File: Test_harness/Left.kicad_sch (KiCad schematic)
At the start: 126 parts

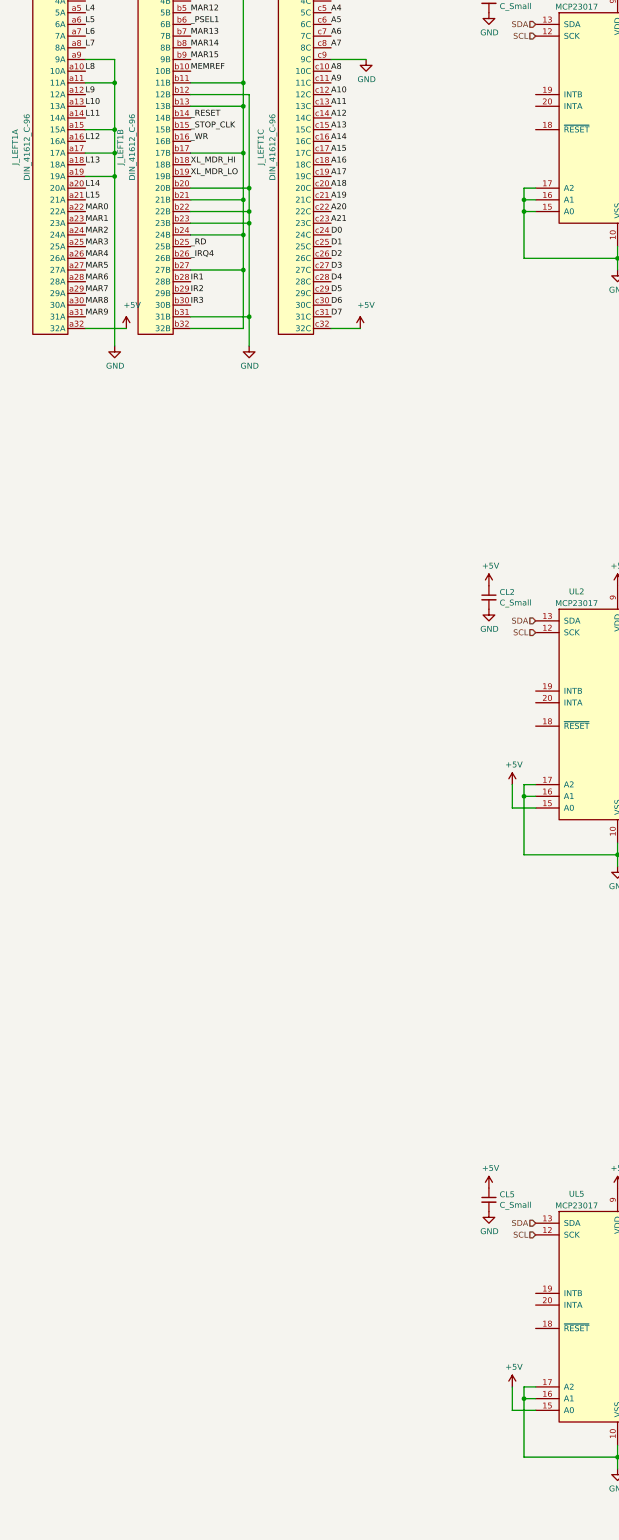
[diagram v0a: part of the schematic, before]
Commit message: route the left connector of test_harness board
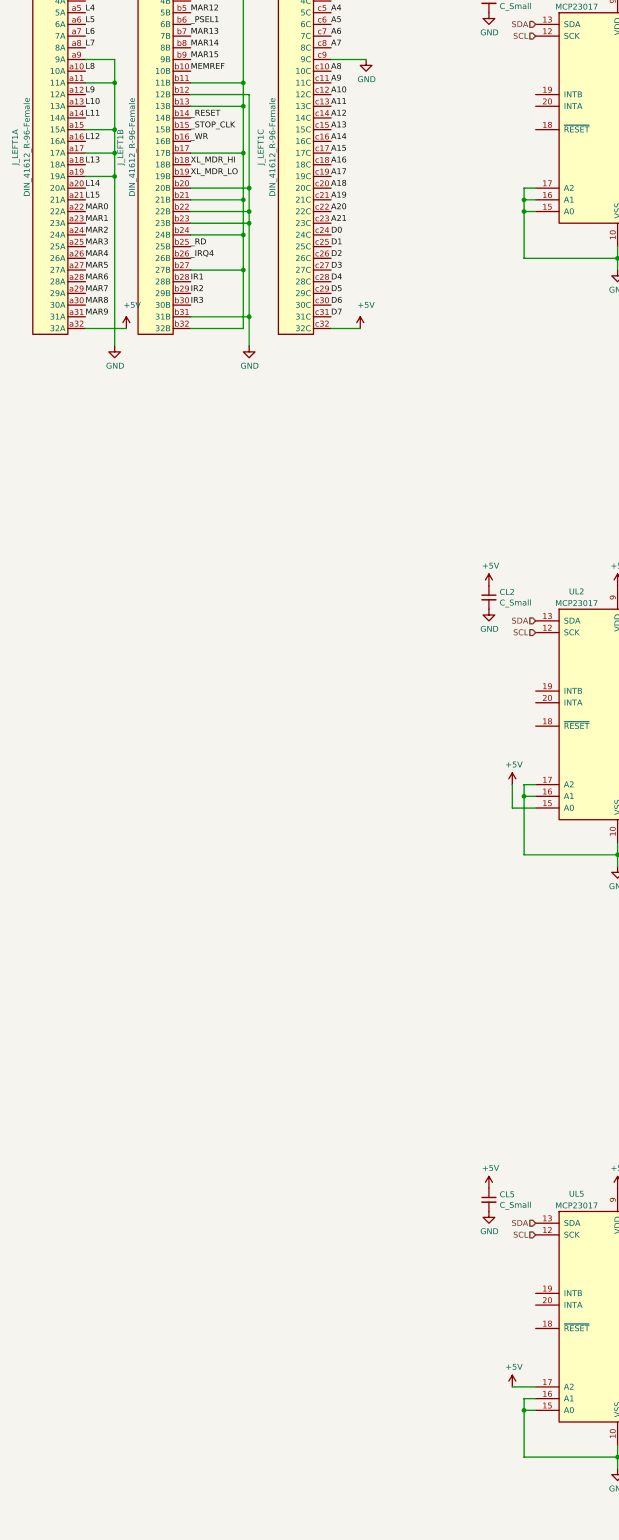
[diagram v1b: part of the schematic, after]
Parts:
- CL1, CL1_1, CL1_2, CL2, CL2_1, CL2_2, CL3, CL3_1, CL3_2, CL4, CL4_1, CL4_2, CL5, CL5_1, CL5_2: footprint Capacitor_SMD:C_1206_3216Metric -> Capacitor_SMD:C_0805_2012Metric
- J_LEFT1: value DIN_41612_C-96 -> DIN_41612_R-96-Female
- UL2: footprint Package_SO:SOIC-28W_7.5x17.9mm_P1.27mm -> Package_SO:TSSOP-28_4.4x9.7mm_P0.65mm
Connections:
- net +5V: now also UL5.17 (A2); no longer UL5.15 (A0)
- net GND: now also UL5.15 (A0); no longer UL5.17 (A2)
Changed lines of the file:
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@@
   (junction (at 128.27 69.85) (diameter 1.016) (color 0 0 0 0))
   (junction (at 128.27 196.85) (diameter 1.016) (color 0 0 0 0))
-  (junction (at 128.27 327.66) (diameter 1.016) (color 0 0 0 0))
+  (junction (at 128.27 330.2) (diameter 1.016) (color 0 0 0 0))
   (junction (at 148.59 80.01) (diameter 1.016) (color 0 0 0 0))
   (junction (at 148.59 209.55) (diameter 1.016) (color 0 0 0 0))
@@
     (stroke (width 0) (type solid) (color 0 0 0 0))
   )
-  (wire (pts (xy 125.73 325.12) (xy 125.73 330.2))
+  (wire (pts (xy 125.73 325.12) (xy 130.81 325.12))
     (stroke (width 0) (type solid) (color 0 0 0 0))
   )
@@
     (stroke (width 0) (type solid) (color 0 0 0 0))
   )
-  (wire (pts (xy 128.27 325.12) (xy 128.27 327.66))
+  (wire (pts (xy 128.27 327.66) (xy 128.27 330.2))
     (stroke (width 0) (type solid) (color 0 0 0 0))
   )
-  (wire (pts (xy 128.27 327.66) (xy 128.27 340.36))
+  (wire (pts (xy 128.27 327.66) (xy 130.81 327.66))
     (stroke (width 0) (type solid) (color 0 0 0 0))
   )
-  (wire (pts (xy 128.27 327.66) (xy 130.81 327.66))
+  (wire (pts (xy 128.27 330.2) (xy 128.27 340.36))
+    (stroke (width 0) (type solid) (color 0 0 0 0))
+  )
+  (wire (pts (xy 128.27 330.2) (xy 130.81 330.2))
     (stroke (width 0) (type solid) (color 0 0 0 0))
   )
@@
     (stroke (width 0) (type solid) (color 0 0 0 0))
   )
-  (wire (pts (xy 130.81 325.12) (xy 128.27 325.12))
-    (stroke (width 0) (type solid) (color 0 0 0 0))
-  )
-  (wire (pts (xy 130.81 330.2) (xy 125.73 330.2))
-    (stroke (width 0) (type solid) (color 0 0 0 0))
-  )
   (wire (pts (xy 148.59 77.47) (xy 148.59 80.01))
     (stroke (width 0) (type solid) (color 0 0 0 0))
@@
       (effects (font (size 1.27 1.27)) (justify left))
     )
-    (property "Footprint" "Capacitor_SMD:C_1206_3216Metric" (id 2) (at 120.65 24.13 0)
+    (property "Footprint" "Capacitor_SMD:C_0805_2012Metric" (id 2) (at 120.65 24.13 0)
       (effects (font (size 1.27 1.27)) hide)
     )
@@
       (effects (font (size 1.27 1.27)) (justify left))
     )
-    (property "Footprint" "Capacitor_SMD:C_1206_3216Metric" (id 2) (at 120.65 153.67 0)
+    (property "Footprint" "Capacitor_SMD:C_0805_2012Metric" (id 2) (at 120.65 153.67 0)
       (effects (font (size 1.27 1.27)) hide)
     )
@@
       (effects (font (size 1.27 1.27)) (justify left))
     )
-    (property "Footprint" "Capacitor_SMD:C_1206_3216Metric" (id 2) (at 120.65 284.48 0)
+    (property "Footprint" "Capacitor_SMD:C_0805_2012Metric" (id 2) (at 120.65 284.48 0)
       (effects (font (size 1.27 1.27)) hide)
     )
@@
       (effects (font (size 1.27 1.27)) (justify left))
     )
-    (property "Footprint" "Capacitor_SMD:C_1206_3216Metric" (id 2) (at 176.53 21.59 0)
+    (property "Footprint" "Capacitor_SMD:C_0805_2012Metric" (id 2) (at 176.53 21.59 0)
       (effects (font (size 1.27 1.27)) hide)
     )
@@
       (effects (font (size 1.27 1.27)) (justify left))
     )
-    (property "Footprint" "Capacitor_SMD:C_1206_3216Metric" (id 2) (at 176.53 85.09 0)
+    (property "Footprint" "Capacitor_SMD:C_0805_2012Metric" (id 2) (at 176.53 85.09 0)
       (effects (font (size 1.27 1.27)) hide)
     )
@@
       (effects (font (size 1.27 1.27)) (justify left))
     )
-    (property "Footprint" "Capacitor_SMD:C_1206_3216Metric" (id 2) (at 176.53 151.13 0)
+    (property "Footprint" "Capacitor_SMD:C_0805_2012Metric" (id 2) (at 176.53 151.13 0)
       (effects (font (size 1.27 1.27)) hide)
     )
@@
       (effects (font (size 1.27 1.27)) (justify left))
     )
-    (property "Footprint" "Capacitor_SMD:C_1206_3216Metric" (id 2) (at 176.53 214.63 0)
+    (property "Footprint" "Capacitor_SMD:C_0805_2012Metric" (id 2) (at 176.53 214.63 0)
       (effects (font (size 1.27 1.27)) hide)
     )
@@
       (effects (font (size 1.27 1.27)) (justify left))
     )
-    (property "Footprint" "Capacitor_SMD:C_1206_3216Metric" (id 2) (at 185.42 280.67 0)
+    (property "Footprint" "Capacitor_SMD:C_0805_2012Metric" (id 2) (at 185.42 280.67 0)
       (effects (font (size 1.27 1.27)) hide)
     )
@@
       (effects (font (size 1.27 1.27)) (justify left))
     )
-    (property "Footprint" "Capacitor_SMD:C_1206_3216Metric" (id 2) (at 185.42 344.17 0)
+    (property "Footprint" "Capacitor_SMD:C_0805_2012Metric" (id 2) (at 185.42 344.17 0)
       (effects (font (size 1.27 1.27)) hide)
     )
@@
       (effects (font (size 1.27 1.27)) (justify left))
     )
-    (property "Footprint" "Capacitor_SMD:C_1206_3216Metric" (id 2) (at 331.47 26.67 0)
+    (property "Footprint" "Capacitor_SMD:C_0805_2012Metric" (id 2) (at 331.47 26.67 0)
       (effects (font (size 1.27 1.27)) hide)
     )
@@
       (effects (font (size 1.27 1.27)) (justify left))
     )
-    (property "Footprint" "Capacitor_SMD:C_1206_3216Metric" (id 2) (at 331.47 156.21 0)
+    (property "Footprint" "Capacitor_SMD:C_0805_2012Metric" (id 2) (at 331.47 156.21 0)
       (effects (font (size 1.27 1.27)) hide)
     )
@@
       (effects (font (size 1.27 1.27)) (justify left))
     )
-    (property "Footprint" "Capacitor_SMD:C_1206_3216Metric" (id 2) (at 387.35 24.13 0)
+    (property "Footprint" "Capacitor_SMD:C_0805_2012Metric" (id 2) (at 387.35 24.13 0)
       (effects (font (size 1.27 1.27)) hide)
     )
@@
       (effects (font (size 1.27 1.27)) (justify left))
     )
-    (property "Footprint" "Capacitor_SMD:C_1206_3216Metric" (id 2) (at 387.35 87.63 0)
+    (property "Footprint" "Capacitor_SMD:C_0805_2012Metric" (id 2) (at 387.35 87.63 0)
       (effects (font (size 1.27 1.27)) hide)
     )
@@
       (effects (font (size 1.27 1.27)) (justify left))
     )
-    (property "Footprint" "Capacitor_SMD:C_1206_3216Metric" (id 2) (at 387.35 153.67 0)
+    (property "Footprint" "Capacitor_SMD:C_0805_2012Metric" (id 2) (at 387.35 153.67 0)
       (effects (font (size 1.27 1.27)) hide)
     )
@@
       (effects (font (size 1.27 1.27)) (justify left))
     )
-    (property "Footprint" "Capacitor_SMD:C_1206_3216Metric" (id 2) (at 387.35 217.17 0)
+    (property "Footprint" "Capacitor_SMD:C_0805_2012Metric" (id 2) (at 387.35 217.17 0)
       (effects (font (size 1.27 1.27)) hide)
     )
@@
     (in_bom yes) (on_board yes)
     (property "Reference" "J_LEFT1" (id 0) (at 17.78 55.88 90))
-    (property "Value" "DIN_41612_C-96" (id 1) (at 20.32 55.88 90))
+    (property "Value" "DIN_41612_R-96-Female" (id 1) (at 20.32 55.88 90))
     (property "Footprint" "Connector_DIN:DIN41612_C_3x32_Male_Horizontal_THT" (id 2) (at 25.4 54.61 0)
       (effects (font (size 1.27 1.27)) hide)
@@
     (in_bom yes) (on_board yes)
     (property "Reference" "J_LEFT1" (id 0) (at 40.64 55.88 90))
-    (property "Value" "DIN_41612_C-96" (id 1) (at 43.18 55.88 90))
+    (property "Value" "DIN_41612_R-96-Female" (id 1) (at 43.18 55.88 90))
     (property "Footprint" "Connector_DIN:DIN41612_C_3x32_Male_Horizontal_THT" (id 2) (at 48.26 54.61 0)
       (effects (font (size 1.27 1.27)) hide)
@@
     (in_bom yes) (on_board yes)
     (property "Reference" "J_LEFT1" (id 0) (at 71.12 55.88 90))
-    (property "Value" "DIN_41612_C-96" (id 1) (at 73.66 55.88 90))
+    (property "Value" "DIN_41612_R-96-Female" (id 1) (at 73.66 55.88 90))
     (property "Footprint" "Connector_DIN:DIN41612_C_3x32_Male_Horizontal_THT" (id 2) (at 78.74 54.61 0)
       (effects (font (size 1.27 1.27)) hide)
@@
     (property "Reference" "UL2" (id 0) (at 139.7 152.4 0))
     (property "Value" "MCP23017" (id 1) (at 139.7 154.94 0))
-    (property "Footprint" "Package_SO:SOIC-28W_7.5x17.9mm_P1.27mm" (id 2) (at 153.67 204.47 0)
+    (property "Footprint" "Package_SO:TSSOP-28_4.4x9.7mm_P0.65mm" (id 2) (at 153.67 204.47 0)
       (effects (font (size 1.27 1.27)) (justify left) hide)
     )

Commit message: the left connector side of the test harness is in good shape.. even discovered that we can have those HP displays now made by broadcom
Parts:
- added DSP_A0, DSP_A1, DSP_A2, DSP_A3, DSP_A4, DSP_A5, DSP_D0, DSP_D1, DSP_L0, DSP_L1, DSP_L2, DSP_L3: HDSP-0762, Components:HDSP-076x-077x-086x-096x, symbol Magic1_components:HDSP-0762
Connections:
- net +5V: now also DSP_A0.7 (Vcc), DSP_A1.7 (Vcc), DSP_A2.7 (Vcc), DSP_A3.7 (Vcc), DSP_A4.7 (Vcc), DSP_A5.7 (Vcc), DSP_D0.7 (Vcc), DSP_D1.7 (Vcc), DSP_L0.7 (Vcc), DSP_L1.7 (Vcc), DSP_L2.7 (Vcc), DSP_L3.7 (Vcc)
- net D_A0: now also DSP_A0.1 (D1)
- net D_A1: now also DSP_A0.8 (D0)
- net D_A10: now also DSP_A3.3 (D3)
- net D_A11: now also DSP_A3.2 (D2)
- net D_A12: now also DSP_A3.1 (D1)
- net D_A13: now also DSP_A3.8 (D0)
- net D_A14: now also DSP_A4.3 (D3)
- net D_A15: now also DSP_A4.2 (D2)
- net D_A16: now also DSP_A4.1 (D1)
- net D_A17: now also DSP_A4.8 (D0)
- net D_A18: now also DSP_A5.3 (D3)
- net D_A19: now also DSP_A5.2 (D2)
- net D_A2: now also DSP_A1.3 (D3)
- net D_A20: now also DSP_A5.1 (D1)
- net D_A21: now also DSP_A5.8 (D0)
- net D_A3: now also DSP_A1.2 (D2)
- net D_A4: now also DSP_A1.1 (D1)
- net D_A5: now also DSP_A1.8 (D0)
- net D_A6: now also DSP_A2.3 (D3)
- net D_A7: now also DSP_A2.2 (D2)
- net D_A8: now also DSP_A2.1 (D1)
- net D_A9: now also DSP_A2.8 (D0)
- net D_D0: now also DSP_D0.3 (D3)
- net D_D1: now also DSP_D0.2 (D2)
- net D_D2: now also DSP_D0.1 (D1)
- net D_D3: now also DSP_D0.8 (D0)
- net D_D4: now also DSP_D1.3 (D3)
- net D_D5: now also DSP_D1.2 (D2)
- net D_D6: now also DSP_D1.1 (D1)
- net D_D7: now also DSP_D1.8 (D0)
- net D_L0: now also DSP_L0.3 (D3)
- net D_L1: now also DSP_L0.2 (D2)
- net D_L10: now also DSP_L2.1 (D1)
- net D_L11: now also DSP_L2.8 (D0)
- net D_L12: now also DSP_L3.3 (D3)
- net D_L13: now also DSP_L3.2 (D2)
- net D_L14: now also DSP_L3.1 (D1)
- net D_L15: now also DSP_L3.8 (D0)
- net D_L2: now also DSP_L0.1 (D1)
- net D_L3: now also DSP_L0.8 (D0)
- net D_L4: now also DSP_L1.3 (D3)
- net D_L5: now also DSP_L1.2 (D2)
- net D_L6: now also DSP_L1.1 (D1)
- net D_L7: now also DSP_L1.8 (D0)
- net D_L8: now also DSP_L2.3 (D3)
- net D_L9: now also DSP_L2.2 (D2)
- net GND: now also DSP_A0.2 (D2), DSP_A0.3 (D3), DSP_A0.4 (Blk), DSP_A0.6 (GND), DSP_A1.4 (Blk), DSP_A1.6 (GND), DSP_A2.4 (Blk), DSP_A2.6 (GND), DSP_A3.4 (Blk), DSP_A3.6 (GND), DSP_A4.4 (Blk), DSP_A4.6 (GND), DSP_A5.4 (Blk), DSP_A5.6 (GND), DSP_D0.4 (Blk), DSP_D0.6 (GND), DSP_D1.4 (Blk), DSP_D1.6 (GND), DSP_L0.4 (Blk), DSP_L0.6 (GND), DSP_L1.4 (Blk), DSP_L1.6 (GND), DSP_L2.4 (Blk), DSP_L2.6 (GND), DSP_L3.4 (Blk), DSP_L3.6 (GND)
- net at D_A16.1 (K): now also RNL3_1_1.6 (R3.2); no longer RNL3_1_1.7 (R2.2)
- net at D_D6.1 (K): now also RNL4_2_2.6 (R3.2); no longer RNL4_2_2.7 (R2.2)
- net at D_A14.1 (K): now also RNL3_1_1.8 (R1.2); no longer RNL3_1_1.5 (R4.2)
- net at RNL3_2_1.5 (R4.2): now also D_A9.1 (K); no longer D_A6.1 (K)
- net at RNL3_2_1.6 (R3.2): now also D_A8.1 (K); no longer D_A7.1 (K)
- net at RNL3_2_1.7 (R2.2): now also D_A7.1 (K); no longer D_A8.1 (K)
- net at RNL3_2_1.8 (R1.2): now also D_A6.1 (K); no longer D_A9.1 (K)
- net at D_A15.1 (K): now also RNL3_1_1.7 (R2.2); no longer RNL3_1_1.6 (R3.2)
- net at D_A17.1 (K): now also RNL3_1_1.5 (R4.2); no longer RNL3_1_1.8 (R1.2)
- net at D_L3.1 (K): now also RNL1_2_1.5 (R4.2); no longer RNL1_2_1.8 (R1.2)
- net at RNL1_2_2.5 (R4.2): now also D_L7.1 (K); no longer D_L4.1 (K)
- net at RNL1_2_2.6 (R3.2): now also D_L6.1 (K); no longer D_L5.1 (K)
- net at RNL1_2_2.7 (R2.2): now also D_L5.1 (K); no longer D_L6.1 (K)
- net at RNL1_2_2.8 (R1.2): now also D_L4.1 (K); no longer D_L7.1 (K)
- net at D_A0.1 (K): now also RNL4_1_1.8 (R1.2); no longer RNL4_1_1.7 (R2.2)
- net at D_A20.1 (K): now also RNL3_1_2.6 (R3.2); no longer RNL3_1_2.7 (R2.2)
- net at D_D3.1 (K): now also RNL4_2_1.5 (R4.2); no longer RNL4_2_1.8 (R1.2)
- net at RNL1_1_1.5 (R4.2): now also D_L11.1 (K); no longer D_L8.1 (K)
- net at RNL1_1_1.6 (R3.2): now also D_L10.1 (K); no longer D_L9.1 (K)
- net at RNL1_1_1.7 (R2.2): now also D_L9.1 (K); no longer D_L10.1 (K)
- net at RNL1_1_1.8 (R1.2): now also D_L8.1 (K); no longer D_L11.1 (K)
- net at D_A11.1 (K): now also RNL3_2_2.7 (R2.2); no longer RNL3_2_2.6 (R3.2)
- net at D_A1.1 (K): now also RNL4_1_1.7 (R2.2); no longer RNL4_1_1.8 (R1.2)
- net at D_L13.1 (K): now also RNL1_1_2.7 (R2.2); no longer RNL1_1_2.6 (R3.2)
- net at D_A19.1 (K): now also RNL3_1_2.7 (R2.2); no longer RNL3_1_2.6 (R3.2)
- net at D_D7.1 (K): now also RNL4_2_2.5 (R4.2); no longer RNL4_2_2.8 (R1.2)
- net at D_L0.1 (K): now also RNL1_2_1.8 (R1.2); no longer RNL1_2_1.5 (R4.2)
- net at D_D1.1 (K): now also RNL4_2_1.7 (R2.2); no longer RNL4_2_1.6 (R3.2)
- net at D_L12.1 (K): now also RNL1_1_2.8 (R1.2); no longer RNL1_1_2.5 (R4.2)
- net at D_A5.1 (K): now also RNL4_1_2.5 (R4.2); no longer RNL4_1_2.8 (R1.2)
- net at RNL1_2_1.6 (R3.2): now also D_L2.1 (K); no longer D_L1.1 (K)
- net at RNL1_2_1.7 (R2.2): now also D_L1.1 (K); no longer D_L2.1 (K)
- net at D_D5.1 (K): now also RNL4_2_2.7 (R2.2); no longer RNL4_2_2.6 (R3.2)
- net at D_D4.1 (K): now also RNL4_2_2.8 (R1.2); no longer RNL4_2_2.5 (R4.2)
- net at D_A21.1 (K): now also RNL3_1_2.5 (R4.2); no longer RNL3_1_2.8 (R1.2)
- net at D_D2.1 (K): now also RNL4_2_1.6 (R3.2); no longer RNL4_2_1.7 (R2.2)
- net at D_D0.1 (K): now also RNL4_2_1.8 (R1.2); no longer RNL4_2_1.5 (R4.2)
- net at D_A4.1 (K): now also RNL4_1_2.6 (R3.2); no longer RNL4_1_2.7 (R2.2)
- net at D_A12.1 (K): now also RNL3_2_2.6 (R3.2); no longer RNL3_2_2.7 (R2.2)
- net at D_A2.1 (K): now also RNL4_1_2.8 (R1.2); no longer RNL4_1_2.5 (R4.2)
- net at D_A3.1 (K): now also RNL4_1_2.7 (R2.2); no longer RNL4_1_2.6 (R3.2)
- net at D_A10.1 (K): now also RNL3_2_2.8 (R1.2); no longer RNL3_2_2.5 (R4.2)
- net at D_A18.1 (K): now also RNL3_1_2.8 (R1.2); no longer RNL3_1_2.5 (R4.2)
- net at D_L15.1 (K): now also RNL1_1_2.5 (R4.2); no longer RNL1_1_2.8 (R1.2)
- net at D_L14.1 (K): now also RNL1_1_2.6 (R3.2); no longer RNL1_1_2.7 (R2.2)
- net at D_A13.1 (K): now also RNL3_2_2.5 (R4.2); no longer RNL3_2_2.8 (R1.2)
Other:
- moved on the sheet: RNL4_1_1

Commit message: added a bunch of things, including board under test power control
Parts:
- added CDSP_A0, CDSP_A1, CDSP_A2, CDSP_A3, CDSP_A4, CDSP_A5, CDSP_D0, CDSP_D1, CDSP_L0, CDSP_L1, CDSP_L2, CDSP_L3, CDSP_MAR0, CDSP_MAR1, CDSP_MAR2, CDSP_MAR3: C_Small, Capacitor_SMD:C_0805_2012Metric, symbol Device:C_Small
- added DSP_MAR0, DSP_MAR1, DSP_MAR2, DSP_MAR3: HDSP-0762, Components:HDSP-076x-077x-086x-096x, symbol Magic1_components:HDSP-0762
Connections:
- net +5V: now also CDSP_A0.1, CDSP_A1.1, CDSP_A2.1, CDSP_A3.1, CDSP_A4.1, CDSP_A5.1, CDSP_D0.1, CDSP_D1.1, CDSP_L0.1, CDSP_L1.1, CDSP_L2.1, CDSP_L3.1, CDSP_MAR0.1, CDSP_MAR1.1, CDSP_MAR2.1, CDSP_MAR3.1, DSP_MAR0.7 (Vcc), DSP_MAR1.7 (Vcc), DSP_MAR2.7 (Vcc), DSP_MAR3.7 (Vcc); no longer J_LEFT1.a32 (32A), J_LEFT1.b1 (1B), J_LEFT1.b11 (11B), J_LEFT1.b13 (13B), J_LEFT1.b17 (17B), J_LEFT1.b21 (21B), J_LEFT1.b24 (24B), J_LEFT1.b27 (27B), J_LEFT1.b32 (32B), J_LEFT1.c32 (32C)
- net D_MAR0: now also DSP_MAR0.3 (D3)
- net D_MAR1: now also DSP_MAR0.2 (D2)
- net D_MAR10: now also DSP_MAR2.1 (D1)
- net D_MAR11: now also DSP_MAR2.8 (D0)
- net D_MAR12: now also DSP_MAR3.3 (D3)
- net D_MAR13: now also DSP_MAR3.2 (D2)
- net D_MAR14: now also DSP_MAR3.1 (D1)
- net D_MAR15: now also DSP_MAR3.8 (D0)
- net D_MAR2: now also DSP_MAR0.1 (D1)
- net D_MAR3: now also DSP_MAR0.8 (D0)
- net D_MAR4: now also DSP_MAR1.3 (D3)
- net D_MAR5: now also DSP_MAR1.2 (D2)
- net D_MAR6: now also DSP_MAR1.1 (D1)
- net D_MAR7: now also DSP_MAR1.8 (D0)
- net D_MAR8: now also DSP_MAR2.3 (D3)
- net D_MAR9: now also DSP_MAR2.2 (D2)
- net GND: now also CDSP_A0.2, CDSP_A1.2, CDSP_A2.2, CDSP_A3.2, CDSP_A4.2, CDSP_A5.2, CDSP_D0.2, CDSP_D1.2, CDSP_L0.2, CDSP_L1.2, CDSP_L2.2, CDSP_L3.2, CDSP_MAR0.2, CDSP_MAR1.2, CDSP_MAR2.2, CDSP_MAR3.2, DSP_MAR0.4 (Blk), DSP_MAR0.6 (GND), DSP_MAR1.4 (Blk), DSP_MAR1.6 (GND), DSP_MAR2.4 (Blk), DSP_MAR2.6 (GND), DSP_MAR3.4 (Blk), DSP_MAR3.6 (GND)
- net at D_MAR0.1 (K): now also RNL2_2_1.8 (R1.2); no longer RNL2_2_1.5 (R4.2)
- net at D_MAR1.1 (K): now also RNL2_2_1.7 (R2.2); no longer RNL2_2_1.6 (R3.2)
- net at D_MAR15.1 (K): now also RNL2_1_2.5 (R4.2); no longer RNL2_1_2.8 (R1.2)
- net at D_MAR10.1 (K): now also RNL2_1_1.6 (R3.2); no longer RNL2_1_1.7 (R2.2)
- net at D_MAR9.1 (K): now also RNL2_1_1.7 (R2.2); no longer RNL2_1_1.6 (R3.2)
- net at D_MAR11.1 (K): now also RNL2_1_1.5 (R4.2); no longer RNL2_1_1.8 (R1.2)
- net at D_MAR2.1 (K): now also RNL2_2_1.6 (R3.2); no longer RNL2_2_1.7 (R2.2)
- net at D_MAR14.1 (K): now also RNL2_1_2.6 (R3.2); no longer RNL2_1_2.7 (R2.2)
- net at D_MAR8.1 (K): now also RNL2_1_1.8 (R1.2); no longer RNL2_1_1.5 (R4.2)
- net at D_MAR6.1 (K): now also RNL2_2_2.6 (R3.2); no longer RNL2_2_2.7 (R2.2)
- net at D_MAR4.1 (K): now also RNL2_2_2.8 (R1.2); no longer RNL2_2_2.5 (R4.2)
- net at D_MAR3.1 (K): now also RNL2_2_1.5 (R4.2); no longer RNL2_2_1.8 (R1.2)
- net at D_MAR7.1 (K): now also RNL2_2_2.5 (R4.2); no longer RNL2_2_2.8 (R1.2)
- net at D_MAR12.1 (K): now also RNL2_1_2.8 (R1.2); no longer RNL2_1_2.5 (R4.2)
- net at D_MAR13.1 (K): now also RNL2_1_2.7 (R2.2); no longer RNL2_1_2.6 (R3.2)
- net at D_MAR5.1 (K): now also RNL2_2_2.7 (R2.2); no longer RNL2_2_2.6 (R3.2)
- new net BRD_POWER: J_LEFT1.a32 (32A), J_LEFT1.b1 (1B), J_LEFT1.b11 (11B), J_LEFT1.b13 (13B), J_LEFT1.b17 (17B), J_LEFT1.b21 (21B), J_LEFT1.b24 (24B), J_LEFT1.b27 (27B), J_LEFT1.b32 (32B), J_LEFT1.c32 (32C)
